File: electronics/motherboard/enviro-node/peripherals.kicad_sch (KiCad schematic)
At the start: 9 parts, among them J5 ST1W008S4AR1500, J6 2604-3105, Q3 BSS214NW, U3 TCA9534

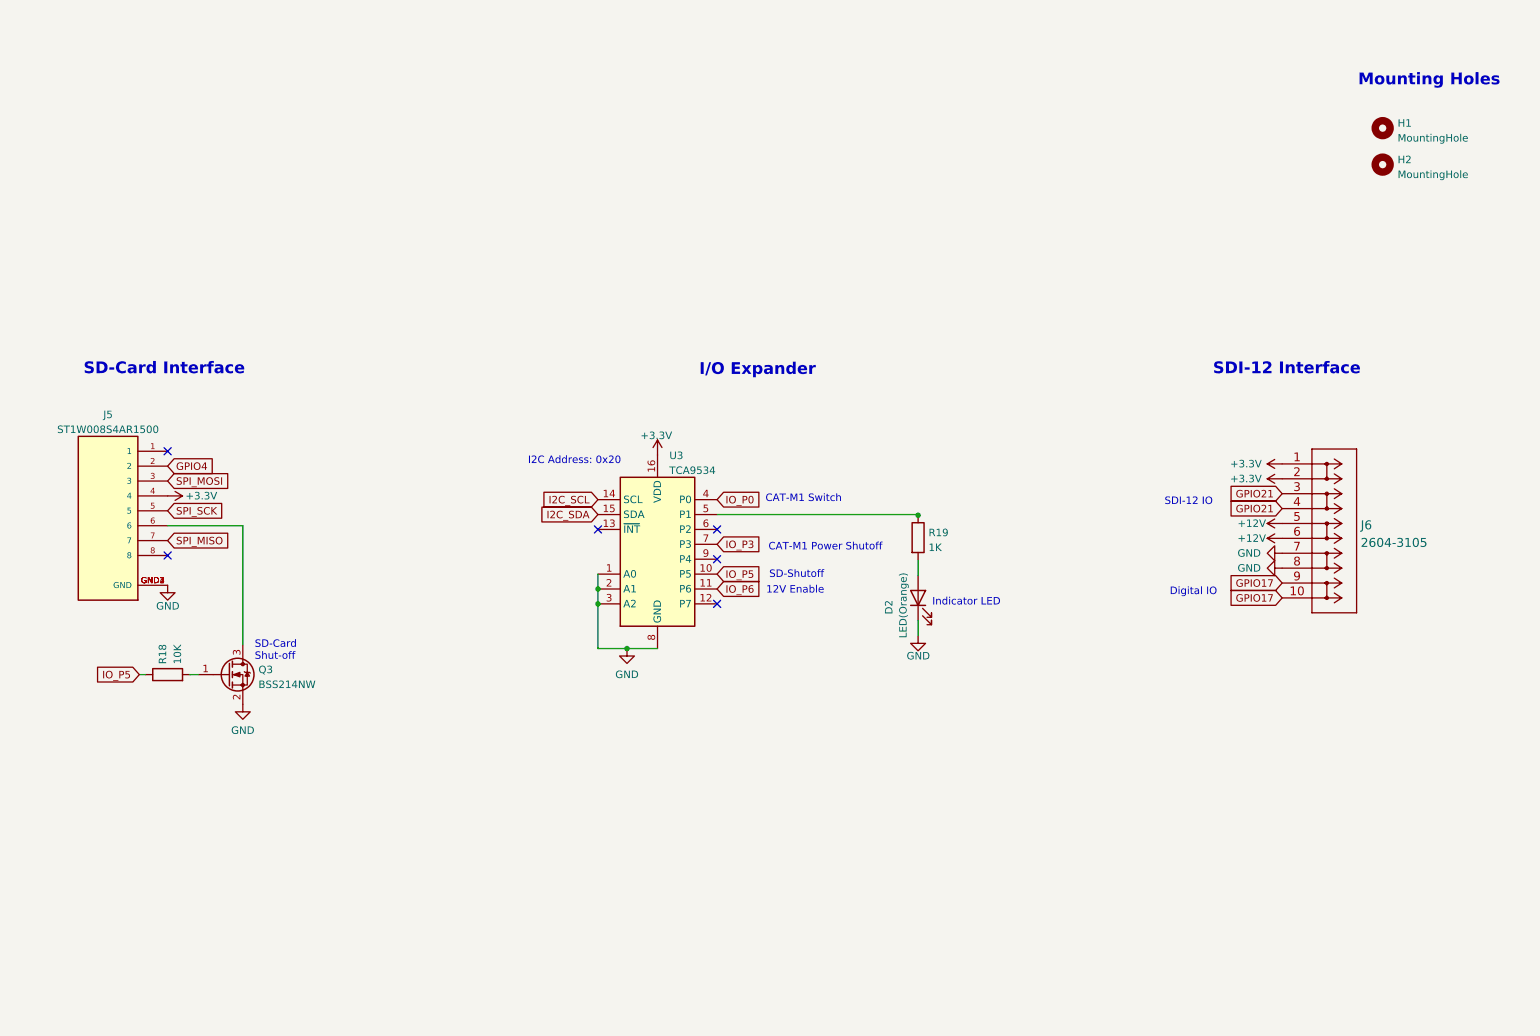
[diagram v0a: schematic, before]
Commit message: fixed unexposed copper pad on inductor and added zipped step file of the motherboard
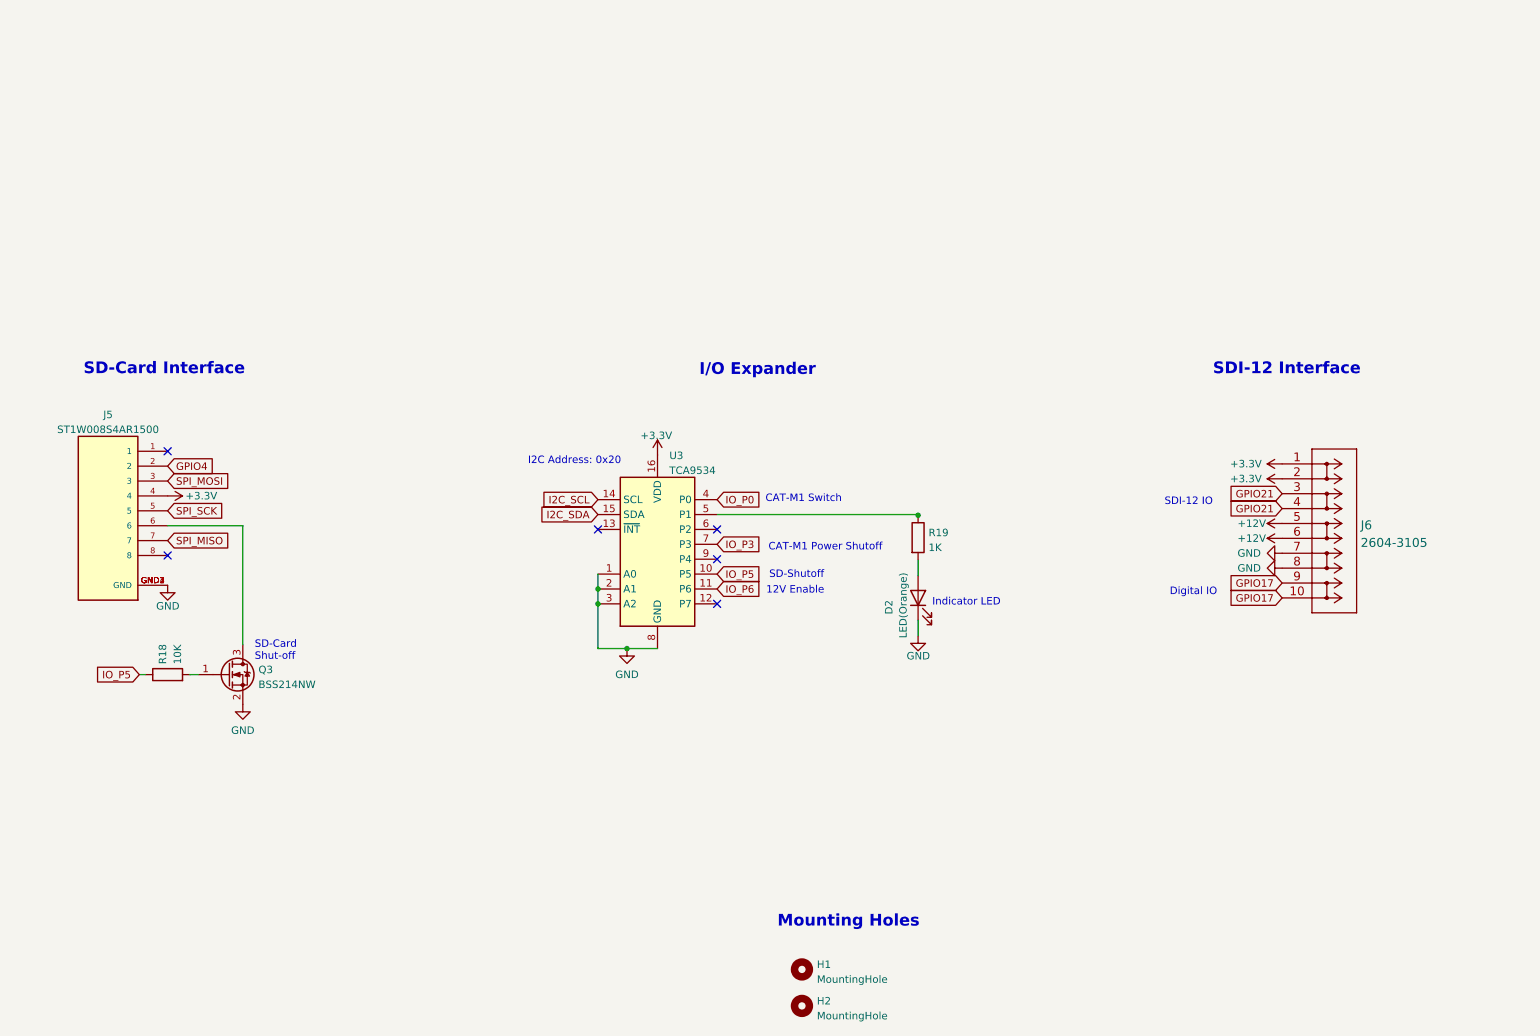
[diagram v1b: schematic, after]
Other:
- moved on the sheet: H1, H2
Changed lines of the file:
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@@
     (effects (font (size 1.27 1.27)) (justify left bottom))
   )
-  (text "Mounting Holes" (at 249.174 30.099 0)
+  (text "Mounting Holes" (at 150.114 173.609 0)
     (effects (font (size 2 2) (thickness 0.4) bold) (justify left bottom))
   )
@@
     (pin "9")
   )
-  (symbol (lib_id "Mechanical:MountingHole") (at 253.365 37.084 0) (unit 1)
-    (in_bom yes) (on_board yes) (fields_autoplaced)
-    (property "Reference" "H1" (id 0) (at 255.905 36.2493 0)
-      (effects (font (size 1.27 1.27)) (justify left))
-    )
-    (property "Value" "MountingHole" (id 1) (at 255.905 38.7862 0)
-      (effects (font (size 1.27 1.27)) (justify left))
-    )
-    (property "Footprint" "MountingHole:MountingHole_4.3x6.2mm_M4_Pad_Via" (id 2) (at 253.365 37.084 0)
-      (effects (font (size 1.27 1.27)) hide)
-    )
-    (property "Datasheet" "~" (id 3) (at 253.365 37.084 0)
+  (symbol (lib_id "Mechanical:MountingHole") (at 154.305 180.594 0) (unit 1)
+    (in_bom yes) (on_board yes) (fields_autoplaced)
+    (property "Reference" "H1" (id 0) (at 156.845 179.7593 0)
+      (effects (font (size 1.27 1.27)) (justify left))
+    )
+    (property "Value" "MountingHole" (id 1) (at 156.845 182.2962 0)
+      (effects (font (size 1.27 1.27)) (justify left))
+    )
+    (property "Footprint" "MountingHole:MountingHole_4.3x6.2mm_M4_Pad_Via" (id 2) (at 154.305 180.594 0)
+      (effects (font (size 1.27 1.27)) hide)
+    )
+    (property "Datasheet" "~" (id 3) (at 154.305 180.594 0)
       (effects (font (size 1.27 1.27)) hide)
     )
@@
     (pin "2")
   )
-  (symbol (lib_id "Mechanical:MountingHole") (at 253.365 43.307 0) (unit 1)
-    (in_bom yes) (on_board yes) (fields_autoplaced)
-    (property "Reference" "H2" (id 0) (at 255.905 42.4723 0)
-      (effects (font (size 1.27 1.27)) (justify left))
-    )
-    (property "Value" "MountingHole" (id 1) (at 255.905 45.0092 0)
-      (effects (font (size 1.27 1.27)) (justify left))
-    )
-    (property "Footprint" "MountingHole:MountingHole_4.3x6.2mm_M4_Pad_Via" (id 2) (at 253.365 43.307 0)
-      (effects (font (size 1.27 1.27)) hide)
-    )
-    (property "Datasheet" "~" (id 3) (at 253.365 43.307 0)
-      (effects (font (size 1.27 1.27)) hide)
-    )
+  (symbol (lib_id "Mechanical:MountingHole") (at 154.305 186.817 0) (unit 1)
+    (in_bom yes) (on_board yes) (fields_autoplaced)
+    (property "Reference" "H2" (id 0) (at 156.845 185.9823 0)
+      (effects (font (size 1.27 1.27)) (justify left))
+    )
+    (property "Value" "MountingHole" (id 1) (at 156.845 188.5192 0)
+      (effects (font (size 1.27 1.27)) (justify left))
+    )
+    (property "Footprint" "MountingHole:MountingHole_4.3x6.2mm_M4_Pad_Via" (id 2) (at 154.305 186.817 0)
+      (effects (font (size 1.27 1.27)) hide)
+    )
+    (property "Datasheet" "~" (id 3) (at 154.305 186.817 0)
+      (effects (font (size 1.27 1.27)) hide)
+    )

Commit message: updated electronics for production
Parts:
- added R42: 0, Resistor_SMD:R_0805_2012Metric, symbol Device:R
- added R43: 10K, Resistor_SMD:R_0805_2012Metric, symbol Device:R
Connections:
- net +3.3V: now also R42.1
- net GND: now also R43.2
- net GPIO17: now also R42.2, R43.1
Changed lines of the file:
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@@
   (junction (at 119.507 115.697) (diameter 0) (color 0 0 0 0)
   )
+  (junction (at 230.632 116.078) (diameter 0) (color 0 0 0 0)
+  )
+  (junction (at 213.995 116.078) (diameter 0) (color 0 0 0 0)
+  )
   (junction (at 119.507 118.237) (diameter 0) (color 0 0 0 0)
   )
   (junction (at 174.117 103.124) (diameter 0) (color 0 0 0 0)
+  )
+  (junction (at 218.313 116.078) (diameter 0) (color 0 0 0 0)
+  )
+  (junction (at 236.22 116.078) (diameter 0) (color 0 0 0 0)
   )
   (no_connect (at 119.507 105.537))
@@
     (stroke (width 0) (type default) (color 0 0 0 0))
   )
+  (wire (pts (xy 236.22 114.681) (xy 236.22 116.078))
+    (stroke (width 0) (type default) (color 0 0 0 0))
+  )
+  (wire (pts (xy 213.995 116.078) (xy 213.995 117.221))
+    (stroke (width 0) (type default) (color 0 0 0 0))
+  )
   (wire (pts (xy 58.928 104.902) (xy 46.101 104.902))
     (stroke (width 0) (type default) (color 0 0 0 0))
   )
+  (wire (pts (xy 213.995 116.078) (xy 218.313 116.078))
+    (stroke (width 0) (type default) (color 0 0 0 0))
+  )
   (wire (pts (xy 174.117 102.997) (xy 174.117 103.124))
     (stroke (width 0) (type default) (color 0 0 0 0))
@@
     (stroke (width 0) (type default) (color 0 0 0 0))
   )
+  (wire (pts (xy 236.22 116.078) (xy 236.22 117.221))
+    (stroke (width 0) (type default) (color 0 0 0 0))
+  )
+  (wire (pts (xy 230.632 116.078) (xy 236.22 116.078))
+    (stroke (width 0) (type default) (color 0 0 0 0))
+  )
   (wire (pts (xy 58.928 125.222) (xy 58.928 104.902))
     (stroke (width 0) (type default) (color 0 0 0 0))
   )
+  (wire (pts (xy 218.313 116.078) (xy 230.632 116.078))
+    (stroke (width 0) (type default) (color 0 0 0 0))
+  )
   (wire (pts (xy 139.827 102.997) (xy 174.117 102.997))
     (stroke (width 0) (type default) (color 0 0 0 0))
   )
+  (wire (pts (xy 213.995 114.681) (xy 213.995 116.078))
+    (stroke (width 0) (type default) (color 0 0 0 0))
+  )
   (wire (pts (xy 119.507 115.697) (xy 119.507 118.237))
     (stroke (width 0) (type default) (color 0 0 0 0))
@@
     (stroke (width 0) (type default) (color 0 0 0 0))
   )
-  (text "Digital IO" (at 217.043 116.967 0)
+  (text "Digital IO" (at 194.818 116.967 0)
     (effects (font (size 1.27 1.27)) (justify left bottom))
   )
@@
     )
   )
-  (global_label "GPIO17" (shape input) (at 236.22 114.681 180) (fields_autoplaced)
-    (effects (font (size 1.27 1.27)) (justify right))
-    (property "Intersheet References" "${INTERSHEET_REFS}" (id 0) (at 226.9126 114.6016 0)
+  (global_label "GPIO17" (shape input) (at 213.995 114.681 180) (fields_autoplaced)
+    (effects (font (size 1.27 1.27)) (justify right))
+    (property "Intersheet References" "${INTERSHEET_REFS}" (id 0) (at 204.6876 114.6016 0)
       (effects (font (size 1.27 1.27)) (justify right) hide)
     )
@@
     )
   )
-  (global_label "GPIO17" (shape input) (at 236.22 117.221 180) (fields_autoplaced)
-    (effects (font (size 1.27 1.27)) (justify right))
-    (property "Intersheet References" "${INTERSHEET_REFS}" (id 0) (at 226.9126 117.1416 0)
+  (global_label "GPIO17" (shape input) (at 213.995 117.221 180) (fields_autoplaced)
+    (effects (font (size 1.27 1.27)) (justify right))
+    (property "Intersheet References" "${INTERSHEET_REFS}" (id 0) (at 204.6876 117.1416 0)
       (effects (font (size 1.27 1.27)) (justify right) hide)
     )
@@
     (pin "2")
     (pin "3")
+  )
+  (symbol (lib_id "Device:R") (at 218.313 112.268 0) (unit 1)
+    (in_bom yes) (on_board yes)
+    (property "Reference" "R42" (id 0) (at 220.091 111.4333 0)
+      (effects (font (size 1.27 1.27)) (justify left))
+    )
+    (property "Value" "0" (id 1) (at 220.091 113.9702 0)
+      (effects (font (size 1.27 1.27)) (justify left))
+    )
+    (property "Footprint" "Resistor_SMD:R_0805_2012Metric" (id 2) (at 216.535 112.268 90)
+      (effects (font (size 1.27 1.27)) hide)
+    )
+    (property "Datasheet" "~" (id 3) (at 218.313 112.268 0)
+      (effects (font (size 1.27 1.27)) hide)
+    )
+    (property "Populate" "False" (id 4) (at 218.313 112.268 0)
+      (effects (font (size 1.27 1.27)) hide)
+    )
+    (pin "1")
+    (pin "2")
   )
   (symbol (lib_id "power:+12V") (at 236.22 107.061 90) (unit 1)
@@
     (pin "1")
   )
+  (symbol (lib_id "power:+3.3V") (at 218.313 108.458 0) (unit 1)
+    (in_bom yes) (on_board yes)
+    (property "Reference" "#PWR0117" (id 0) (at 218.313 112.268 0)
+      (effects (font (size 1.27 1.27)) hide)
+    )
+    (property "Value" "+3.3V" (id 1) (at 221.234 105.029 0)
+      (effects (font (size 1.27 1.27)) (justify right))
+    )
+    (property "Footprint" "" (id 2) (at 218.313 108.458 0)
+      (effects (font (size 1.27 1.27)) hide)
+    )
+    (property "Datasheet" "" (id 3) (at 218.313 108.458 0)
+      (effects (font (size 1.27 1.27)) hide)
+    )
+    (pin "1")
+  )
+  (symbol (lib_id "power:GND") (at 230.632 123.698 0) (unit 1)
+    (in_bom yes) (on_board yes)
+    (property "Reference" "#PWR0116" (id 0) (at 230.632 130.048 0)
+      (effects (font (size 1.27 1.27)) hide)
+    )
+    (property "Value" "GND" (id 1) (at 228.727 127.254 0)
+      (effects (font (size 1.27 1.27)) (justify left))
+    )
+    (property "Footprint" "" (id 2) (at 230.632 123.698 0)
+      (effects (font (size 1.27 1.27)) hide)
+    )
+    (property "Datasheet" "" (id 3) (at 230.632 123.698 0)
+      (effects (font (size 1.27 1.27)) hide)
+    )
+    (pin "1")
+  )
   (symbol (lib_id "power:GND") (at 236.22 112.141 270) (unit 1)
     (in_bom yes) (on_board yes)
@@
       (effects (font (size 1.27 1.27)) hide)
     )
+    (pin "1")
+    (pin "2")
+  )
+  (symbol (lib_id "Device:R") (at 230.632 119.888 0) (unit 1)
+    (in_bom yes) (on_board yes)
+    (property "Reference" "R43" (id 0) (at 232.41 119.0533 0)
+      (effects (font (size 1.27 1.27)) (justify left))
+    )
+    (property "Value" "10K" (id 1) (at 232.41 121.5902 0)
+      (effects (font (size 1.27 1.27)) (justify left))
+    )
+    (property "Footprint" "Resistor_SMD:R_0805_2012Metric" (id 2) (at 228.854 119.888 90)
+      (effects (font (size 1.27 1.27)) hide)
+    )
+    (property "Datasheet" "~" (id 3) (at 230.632 119.888 0)
+      (effects (font (size 1.27 1.27)) hide)
+    )

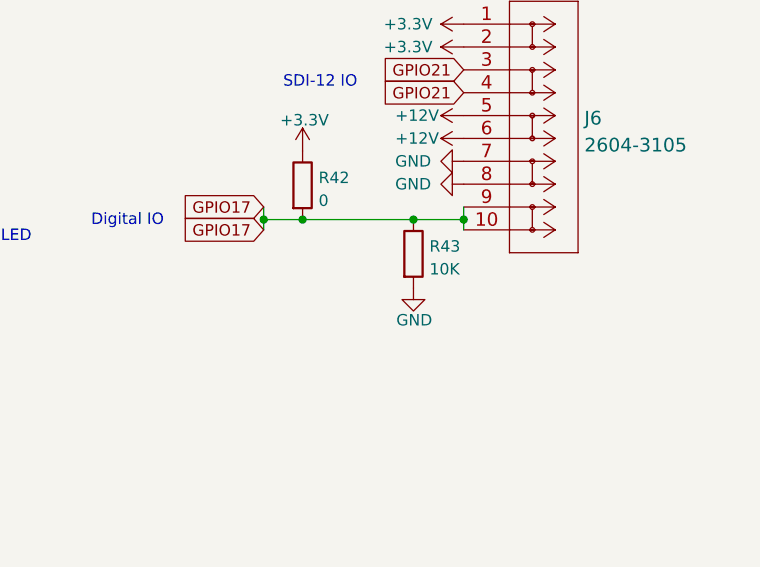
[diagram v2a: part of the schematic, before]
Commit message: Fixed most errors on the 1.0.1 board revision, resolved ERC errors. No PCB work in this commit.
1. Added a solder jumper in-line with with the USB/UART bridge TX pin. If this jumper is
   broken then the RX pin on the UART header can be used. Note the TX/RX discrepancy here is
   not a typo.

2. Changed the USB/UART bridge power supply wiring so it will not try to power the board
   when a USB cable is plugged in. Batteries must be present.

3. The battery monitor VS/A0/A1 pins put back to +3.3v rather than VBAT so it can be read
   while the battery is being charged via the solar panel.

4. Moved the main 3.3v regulator to after the power switch so it is not running all the time.

5. Reverted the change that swapped the piezo buzzer and rain gauge input pins.

6. Noted that R42 and R43 should not be populated during manufacture.

7. Changed the part number for the USB-C LiPo charger to MCP73832T-2ACI/OT.

8. Resolved all KiCAD ERC errors on the schematics. These were all related to KiCAD not
   knowing where power was coming from or IC power pins not being correctly defined in
   the components. Warnings were not checked.
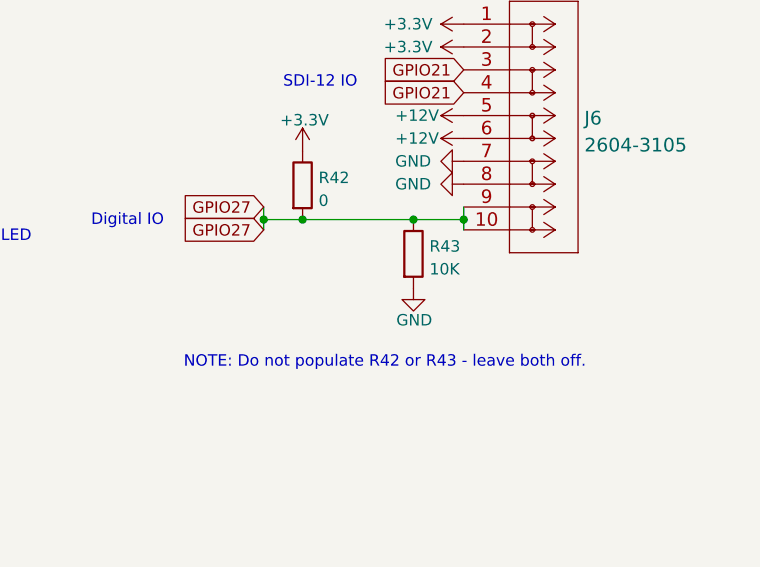
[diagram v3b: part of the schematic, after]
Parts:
- R42: now left out of the parts list
- R43: Populate (none) -> False; now left out of the parts list
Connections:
- net GPIO17 renamed GPIO27
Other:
- note added: "NOTE: Do not populate R42 or R43 - leave both off."
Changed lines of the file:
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@@
+    (effects (font (size 1.27 1.27)) (justify left bottom))
+  )
+  (text "NOTE: Do not populate R42 or R43 - leave both off."
+    (at 205.105 132.715 0)
     (effects (font (size 1.27 1.27)) (justify left bottom))
   )
@@
     )
   )
-  (global_label "GPIO17" (shape input) (at 213.995 114.681 180) (fields_autoplaced)
+  (global_label "GPIO27" (shape input) (at 213.995 114.681 180) (fields_autoplaced)
     (effects (font (size 1.27 1.27)) (justify right))
     (property "Intersheet References" "${INTERSHEET_REFS}" (id 0) (at 204.6876 114.6016 0)
@@
     )
   )
-  (global_label "GPIO17" (shape input) (at 213.995 117.221 180) (fields_autoplaced)
+  (global_label "GPIO27" (shape input) (at 213.995 117.221 180) (fields_autoplaced)
     (effects (font (size 1.27 1.27)) (justify right))
     (property "Intersheet References" "${INTERSHEET_REFS}" (id 0) (at 204.6876 117.1416 0)
@@
   )
   (symbol (lib_id "Device:R") (at 218.313 112.268 0) (unit 1)
-    (in_bom yes) (on_board yes)
+    (in_bom no) (on_board yes)
     (property "Reference" "R42" (id 0) (at 220.091 111.4333 0)
       (effects (font (size 1.27 1.27)) (justify left))
@@
   )
   (symbol (lib_id "Device:R") (at 230.632 119.888 0) (unit 1)
-    (in_bom yes) (on_board yes)
+    (in_bom no) (on_board yes)
     (property "Reference" "R43" (id 0) (at 232.41 119.0533 0)
       (effects (font (size 1.27 1.27)) (justify left))
@@
       (effects (font (size 1.27 1.27)) hide)
     )
+    (property "Populate" "False" (id 4) (at 230.632 119.888 0)
+      (effects (font (size 1.27 1.27)) hide)
+    )

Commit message: Last commit did not get changes to C17 & C23, changed them again to 0.1uF.
Changed footprint of optional pull-up/pull-down R42 & R43 to be through-hole.
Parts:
- R42, R43: footprint Resistor_SMD:R_0805_2012Metric -> Resistor_THT:R_Axial_DIN0207_L6.3mm_D2.5mm_P10.16mm_Horizontal
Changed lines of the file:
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@@
       (effects (font (size 1.27 1.27)) (justify left))
     )
-    (property "Footprint" "Resistor_SMD:R_0805_2012Metric" (id 2) (at 216.535 112.268 90)
+    (property "Footprint" "Resistor_THT:R_Axial_DIN0207_L6.3mm_D2.5mm_P10.16mm_Horizontal" (id 2) (at 216.535 112.268 90)
       (effects (font (size 1.27 1.27)) hide)
     )
@@
       (effects (font (size 1.27 1.27)) (justify left))
     )
-    (property "Footprint" "Resistor_SMD:R_0805_2012Metric" (id 2) (at 228.854 119.888 90)
-      (effects (font (size 1.27 1.27)) hide)
-    )
+    (property "Footprint" "Resistor_THT:R_Axial_DIN0207_L6.3mm_D2.5mm_P10.16mm_Horizontal" (id 2) (at 228.854 119.888 90)
+      (effects (font (size 1.27 1.27)) hide)
+    )
